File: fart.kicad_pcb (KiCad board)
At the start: 2 copper layers, 68.6 x 66 mm, 2 parts, among them U1 F3853, X1 CartConn

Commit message: PCB update
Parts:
- added REF**: MountingHole_5.3mm_M5, Mounting_Holes:MountingHole_5.3mm_M5, F.Cu at (118.1, 176.5)
- added REF**: MountingHole_5.3mm_M5, Mounting_Holes:MountingHole_5.3mm_M5, F.Cu at (184.2, 176.5)
- added REF**: MountingHole_5.3mm_M5, Mounting_Holes:MountingHole_5.3mm_M5, F.Cu at (184.2, 99.1)
- added REF**: MountingHole_5.3mm_M5, Mounting_Holes:MountingHole_5.3mm_M5, F.Cu at (118.1, 99.1)
- U1: moved to F.Cu
- moved X1 232.7 mm to (177.8, 67.9)
- moved U1 231.4 mm to (176.5, 95.2), turned to 270 degrees
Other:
- outline, holes or cut-outs redrawn

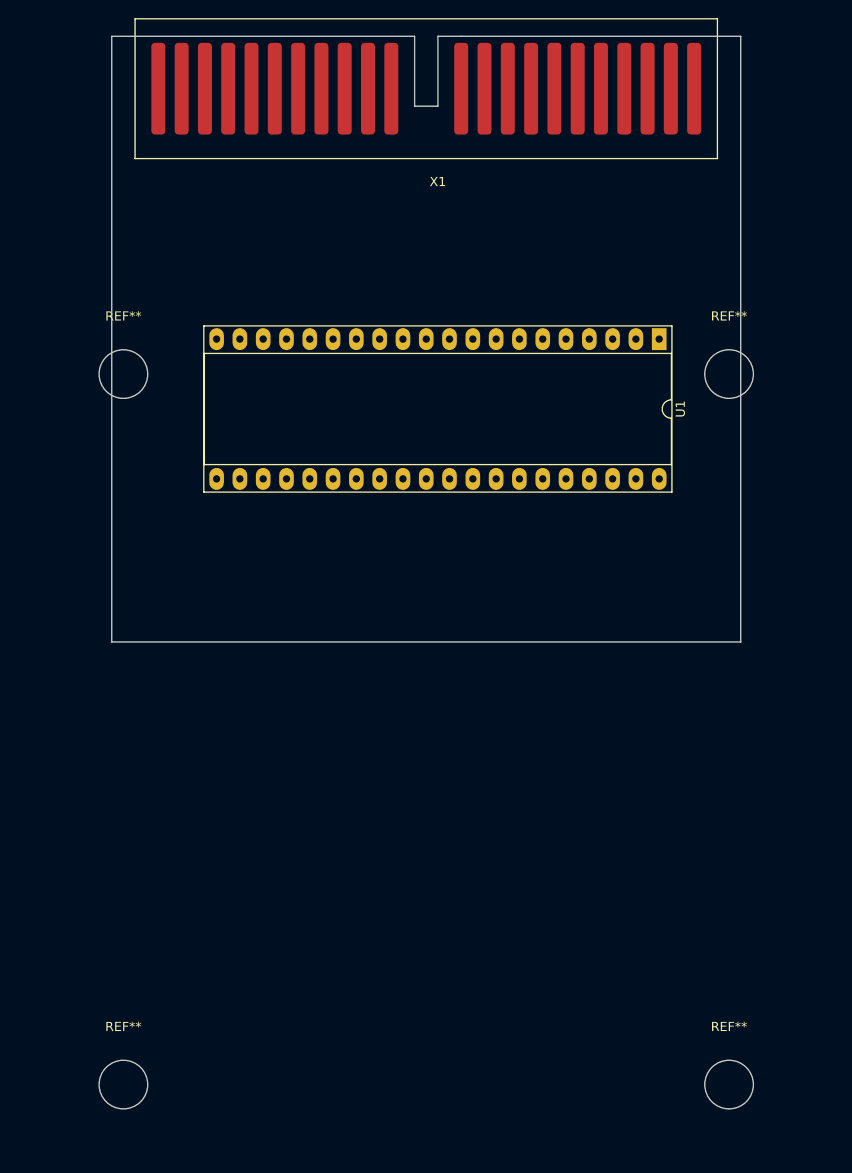
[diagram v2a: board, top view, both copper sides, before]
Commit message: Update PCB and socket 3d model
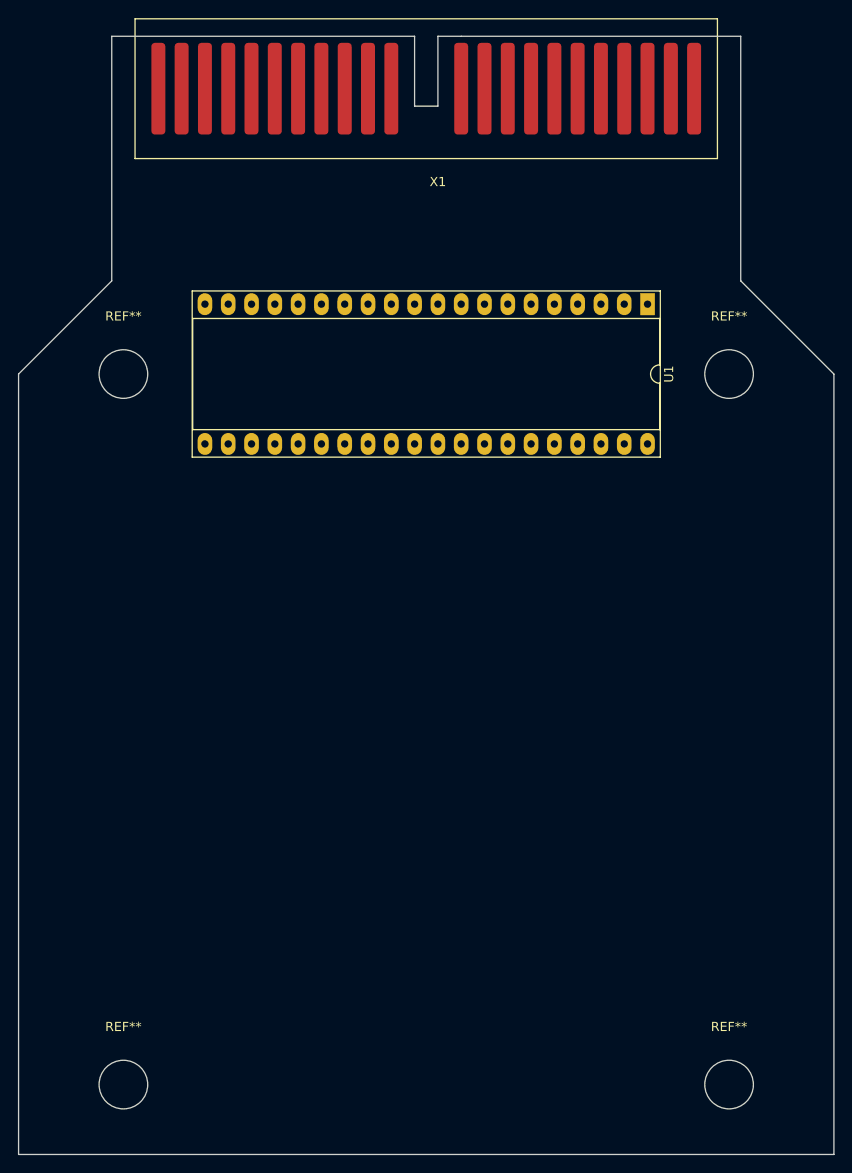
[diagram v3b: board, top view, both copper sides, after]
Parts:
- moved U1 4.02 mm to (175.3, 91.4)
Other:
- board size 68.6 x 66 mm -> 88.9 x 121.9 mm
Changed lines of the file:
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@@
-(kicad_pcb (version 20171130) (host pcbnew 5.1.2-f72e74a~84~ubuntu18.04.1)
+(kicad_pcb (version 20171130) (host pcbnew "(5.1.0)-1")
   (general
     (thickness 1.6)
-    (drawings 9)
+    (drawings 13)
     (tracks 0)
     (zones 0)
@@
   )
   (module Housings_DIP:DIP-40_W15.24mm_Socket_LongPads (layer F.Cu)
-    (at 176.53 95.25 270)
+    (at 175.26 91.44 270)
     (descr "40-lead though-hole mounted DIP package, row spacing 15.24 mm (600 mils), Socket, LongPads")
     (tags "THT DIP DIL PDIP 2.54mm 15.24mm 600mil Socket LongPads")
@@
       (rotate (xyz 0 0 0))
     )
+    (model ${KISYS3DMOD}/Package_DIP.3dshapes/DIP-40_W15.24mm_Socket.step
+      (at (xyz 0 0 0))
+      (scale (xyz 1 1 1))
+      (rotate (xyz 0 0 0))
+    )
   )
   (module fart:Cart_Conn (layer F.Cu)
@@
       (net 4 /ROMC3))
   )
+  (gr_line (start 106.68 99.06) (end 116.84 88.9) (layer Edge.Cuts) (width 0.05))
+  (gr_line (start 106.68 184.15) (end 106.68 99.06) (layer Edge.Cuts) (width 0.05))
+  (gr_line (start 195.58 184.15) (end 106.68 184.15) (layer Edge.Cuts) (width 0.05))
+  (gr_line (start 195.58 99.06) (end 195.58 184.15) (layer Edge.Cuts) (width 0.05))
+  (gr_line (start 185.42 88.9) (end 195.58 99.06) (layer Edge.Cuts) (width 0.05))
   (gr_line (start 152.4 62.23) (end 154.94 62.23) (layer Edge.Cuts) (width 0.05))
   (gr_line (start 152.4 69.85) (end 152.4 62.23) (layer Edge.Cuts) (width 0.05))
@@
   (gr_line (start 154.94 62.23) (end 185.42 62.23) (layer Edge.Cuts) (width 0.05))
   (gr_line (start 149.86 62.23) (end 149.86 69.85) (layer Edge.Cuts) (width 0.05))
-  (gr_line (start 116.84 128.27) (end 116.84 62.23) (layer Edge.Cuts) (width 0.05))
-  (gr_line (start 185.42 128.27) (end 116.84 128.27) (layer Edge.Cuts) (width 0.05))
-  (gr_line (start 185.42 62.23) (end 185.42 128.27) (layer Edge.Cuts) (width 0.05))
+  (gr_line (start 116.84 88.9) (end 116.84 62.23) (layer Edge.Cuts) (width 0.05))
+  (gr_line (start 185.42 62.23) (end 185.42 88.9) (layer Edge.Cuts) (width 0.05))
   (gr_line (start 116.84 62.23) (end 149.86 62.23) (layer Edge.Cuts) (width 0.05))
 )

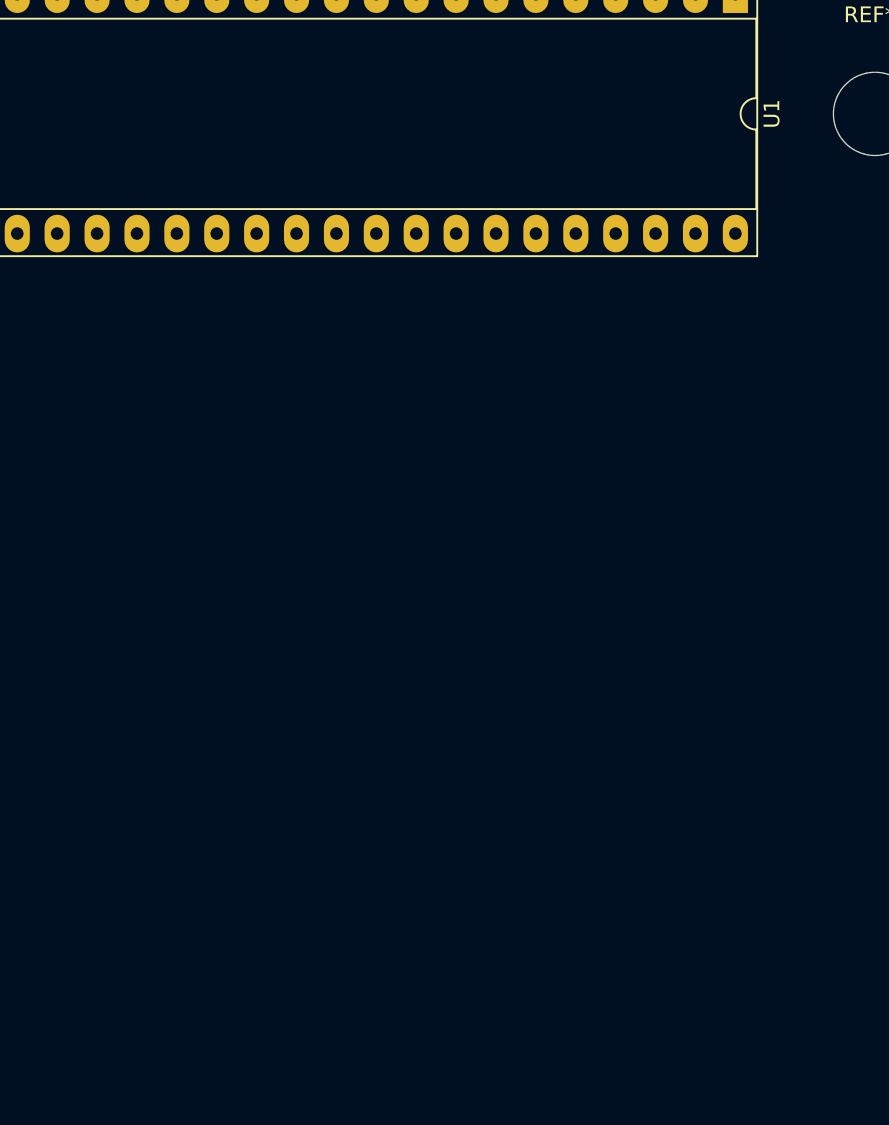
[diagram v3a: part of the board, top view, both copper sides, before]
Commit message: Add EEPROM and address decoder
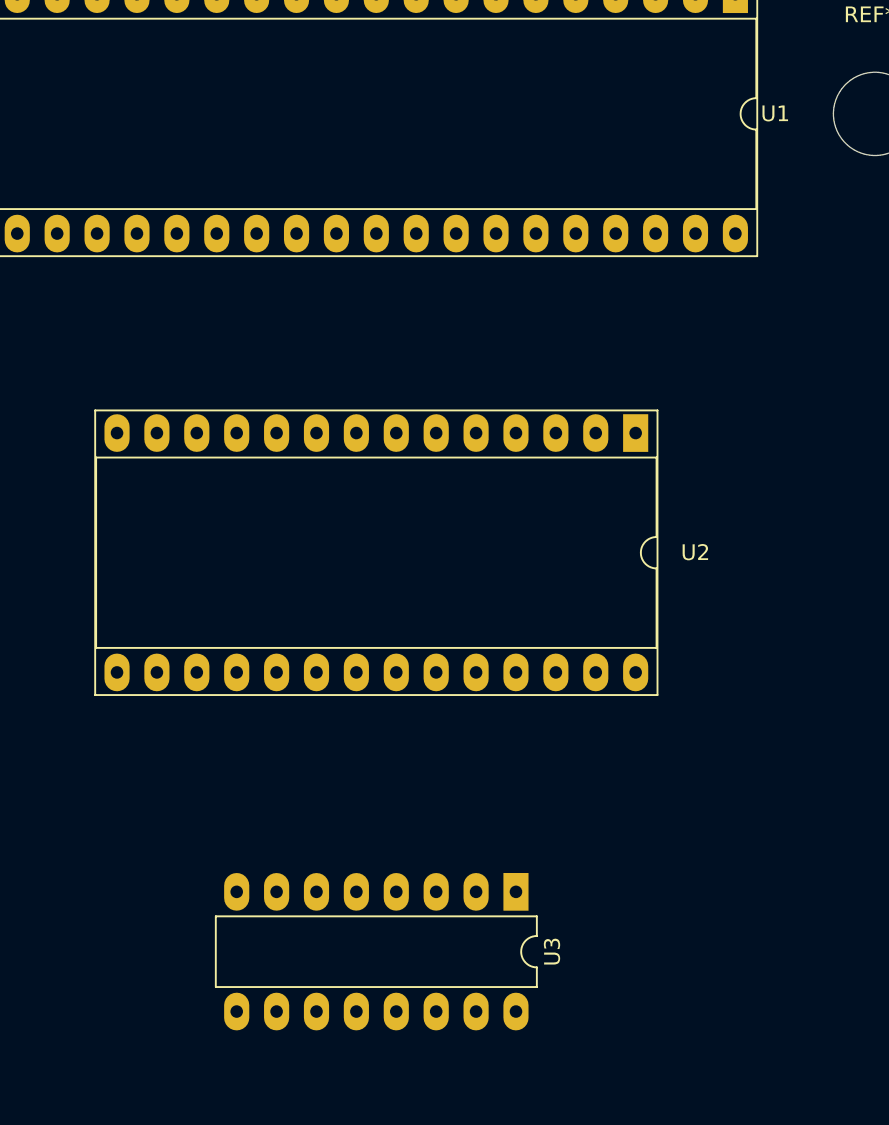
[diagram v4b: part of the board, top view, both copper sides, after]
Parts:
- added U2: AT28C64, Housings_DIP:DIP-28_W15.24mm_Socket_LongPads, F.Cu at (168.9, 119.4)
- added U3: 74156, Housings_DIP:DIP-16_W7.62mm_LongPads, F.Cu at (161.3, 148.6)

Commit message: Massive update
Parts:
- removed U2: AT28C64, Housings_DIP:DIP-28_W15.24mm_Socket_LongPads
- added U4: 74LS00, Housings_DIP:DIP-14_W7.62mm_Socket_LongPads, F.Cu at (121.9, 141.0)
- added U5: AT28C16, Housings_DIP:DIP-24_W15.24mm_Socket_LongPads, F.Cu at (144.8, 134.6)
- X1: moved to B.Cu
- moved U1 51.4 mm to (127.0, 109.2), turned to 90 degrees
- moved U3 47.1 mm to (119.4, 127.0), turned to 90 degrees
- moved X1 1.27 mm to (177.8, 69.2)
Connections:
- U1 pad 10: (no net) -> /A5
- U1 pad 11: (no net) -> /A4
- U1 pad 12: (no net) -> /A3
- U1 pad 13: (no net) -> /A2
- U1 pad 14: (no net) -> /A1
- U1 pad 15: (no net) -> /A0
- U1 pad 25: (no net) -> /A8
- U1 pad 26: (no net) -> /A9
- U1 pad 27: (no net) -> /A10
- U1 pad 28: (no net) -> /A11
- U1 pad 29: (no net) -> /A12
- U1 pad 30: (no net) -> /A13
- U1 pad 31: (no net) -> /A14
- U1 pad 32: (no net) -> /A15
- U1 pad 33: (no net) -> /REGDR
- U1 pad 34: (no net) -> /CPU_READ
- U1 pad 5: (no net) -> /~PRI_IN
- U1 pad 6: (no net) -> /~RAM_WRITE
- U1 pad 7: (no net) -> /~EXT_INT
- U1 pad 8: (no net) -> /A7
- U1 pad 9: (no net) -> /A6
- U3 pad 1: (no net) -> /A13
- U3 pad 10: (no net) -> /28xx
- U3 pad 11: (no net) -> /30xx
- U3 pad 12: (no net) -> /38xx
- U3 pad 13: (no net) -> /A11
- U3 pad 14: (no net) -> GND
- U3 pad 15: (no net) -> /A13
- U3 pad 2: (no net) -> GND
- U3 pad 3: (no net) -> /A12
- U3 pad 4: (no net) -> /18xx
- U3 pad 5: (no net) -> /10xx
- U3 pad 6: (no net) -> /08xx
- U3 pad 7: (no net) -> /00xx
- U3 pad 9: (no net) -> /20xx
- X1 pad 21: (no net) -> Net-(X1-Pad21)
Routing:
- net /WRITE: track 0.00 -> 59.5 mm, vias 0 -> 1
- net /D7: track 0.00 -> 56.0 mm, vias 0 -> 1
- net /D6: track 0.00 -> 55.6 mm, vias 0 -> 1
- net /D5: track 0.00 -> 55.3 mm, vias 0 -> 1
- net /D4: track 0.00 -> 52.4 mm, vias 0 -> 1
- net /PHI: track 0.00 -> 50.9 mm, vias 0 -> 1
- net /ROMC2: track 0.00 -> 48.8 mm, vias 0 -> 1
- net /ROMC3: track 0.00 -> 45.9 mm, vias 0 -> 1
- net /ROMC4: track 0.00 -> 35.3 mm, vias 0 -> 1
- net /D3: track 0.00 -> 33.0 mm, vias 0 -> 1
- net /~INTREQ: track 0.00 -> 6.35 mm, vias 0 -> 1
- net /ROMC1: track 0.00 -> 6.35 mm, vias 0 -> 1
- net /ROMC0: track 0.00 -> 6.35 mm, vias 0 -> 1
- net /D2: track 0.00 -> 6.35 mm, vias 0 -> 1
- net /D1: track 0.00 -> 6.35 mm, vias 0 -> 1
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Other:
- board size 88.9 x 121.9 mm -> 88.9 x 119.4 mm

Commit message: Rough routing done
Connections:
- U4 pad 1: /CPU_READ -> Net-(U4-Pad1)
- U4 pad 11: Net-(U4-Pad11) -> /~CPU_READ
- U4 pad 12: Net-(U4-Pad12) -> /CPU_READ
- U4 pad 13: Net-(U4-Pad13) -> /CPU_READ
- U4 pad 14: +5V -> (no net)
- U4 pad 2: /CPU_READ -> Net-(U4-Pad2)
- U4 pad 3: /~CPU_READ -> Net-(U4-Pad3)
- U4 pad 7: GND -> (no net)
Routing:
- net GND: track 0.00 -> 170.8 mm
- net +5V: track 0.00 -> 132.5 mm
- net /D2: track 6.35 -> 78.1 mm, vias 1 -> 2
- net /D0: track 6.35 -> 72.7 mm, vias 1 -> 2
- net /D1: track 6.35 -> 69.1 mm
- net /CPU_READ: track 0.00 -> 59.3 mm
- net /~INTREQ: track 6.35 -> 65.3 mm
- net /A13: track 0.00 -> 56.7 mm
- net /A12: track 0.00 -> 55.3 mm
- net /A11: track 0.00 -> 47.9 mm
- net +12V: track 0.00 -> 44.9 mm, vias 0 -> 2
- net /A8: track 0.00 -> 43.7 mm
- net /ROMC1: track 6.35 -> 46.9 mm
- net /ROMC0: track 6.35 -> 46.9 mm
- net /A9: track 0.00 -> 37.2 mm
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
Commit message: Update
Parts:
- added C1: 47uF 16V, Capacitors_THT:CP_Radial_D5.0mm_P2.50mm, F.Cu at (116.2, 135.9)
- added C5: 100nF, Capacitors_THT:C_Disc_D5.0mm_W2.5mm_P5.00mm, F.Cu at (141.0, 121.3)
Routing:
- net GND: track 170.8 -> 206.8 mm
- net +5V: track 132.5 -> 140.4 mm

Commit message: Add credentials
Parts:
- added REF**: SolderWirePad_single_0-8mmDrill, Wire_Pads:SolderWirePad_single_0-8mmDrill, F.Cu at (188.0, 109.2)
- added REF**: SolderWirePad_single_0-8mmDrill, Wire_Pads:SolderWirePad_single_0-8mmDrill, F.Cu at (182.9, 124.5)
- added REF**: SolderWirePad_single_0-8mmDrill, Wire_Pads:SolderWirePad_single_0-8mmDrill, F.Cu at (162.6, 170.2)
- added REF**: SolderWirePad_single_0-8mmDrill, Wire_Pads:SolderWirePad_single_0-8mmDrill, F.Cu at (165.1, 170.2)
- added REF**: SolderWirePad_single_0-8mmDrill, Wire_Pads:SolderWirePad_single_0-8mmDrill, F.Cu at (172.7, 170.2)
- added REF**: SolderWirePad_single_0-8mmDrill, Wire_Pads:SolderWirePad_single_0-8mmDrill, F.Cu at (160.0, 170.2)
- added REF**: SolderWirePad_single_0-8mmDrill, Wire_Pads:SolderWirePad_single_0-8mmDrill, F.Cu at (170.2, 170.2)
- added REF**: SolderWirePad_single_0-8mmDrill, Wire_Pads:SolderWirePad_single_0-8mmDrill, F.Cu at (129.5, 170.2)
- added REF**: SolderWirePad_single_0-8mmDrill, Wire_Pads:SolderWirePad_single_0-8mmDrill, F.Cu at (149.9, 170.2)
- added REF**: SolderWirePad_single_0-8mmDrill, Wire_Pads:SolderWirePad_single_0-8mmDrill, F.Cu at (132.1, 170.2)
- added REF**: SolderWirePad_single_0-8mmDrill, Wire_Pads:SolderWirePad_single_0-8mmDrill, F.Cu at (121.9, 170.2)
- added REF**: SolderWirePad_single_0-8mmDrill, Wire_Pads:SolderWirePad_single_0-8mmDrill, F.Cu at (134.6, 170.2)
- added REF**: SolderWirePad_single_0-8mmDrill, Wire_Pads:SolderWirePad_single_0-8mmDrill, F.Cu at (182.9, 116.8)
- added REF**: SolderWirePad_single_0-8mmDrill, Wire_Pads:SolderWirePad_single_0-8mmDrill, F.Cu at (154.9, 170.2)
- added REF**: SolderWirePad_single_0-8mmDrill, Wire_Pads:SolderWirePad_single_0-8mmDrill, F.Cu at (137.2, 170.2)
- added REF**: SolderWirePad_single_0-8mmDrill, Wire_Pads:SolderWirePad_single_0-8mmDrill, F.Cu at (144.8, 170.2)
- added REF**: SolderWirePad_single_0-8mmDrill, Wire_Pads:SolderWirePad_single_0-8mmDrill, F.Cu at (182.9, 137.2)
- added REF**: SolderWirePad_single_0-8mmDrill, Wire_Pads:SolderWirePad_single_0-8mmDrill, F.Cu at (190.5, 137.2)
- added REF**: SolderWirePad_single_0-8mmDrill, Wire_Pads:SolderWirePad_single_0-8mmDrill, F.Cu at (185.4, 137.2)
- added REF**: SolderWirePad_single_0-8mmDrill, Wire_Pads:SolderWirePad_single_0-8mmDrill, F.Cu at (188.0, 137.2)
- added REF**: SolderWirePad_single_0-8mmDrill, Wire_Pads:SolderWirePad_single_0-8mmDrill, F.Cu at (180.3, 137.2)
- added REF**: SolderWirePad_single_0-8mmDrill, Wire_Pads:SolderWirePad_single_0-8mmDrill, F.Cu at (185.4, 139.7)
- added REF**: SolderWirePad_single_0-8mmDrill, Wire_Pads:SolderWirePad_single_0-8mmDrill, F.Cu at (188.0, 139.7)
- added REF**: SolderWirePad_single_0-8mmDrill, Wire_Pads:SolderWirePad_single_0-8mmDrill, F.Cu at (185.4, 119.4)
- added REF**: SolderWirePad_single_0-8mmDrill, Wire_Pads:SolderWirePad_single_0-8mmDrill, F.Cu at (180.3, 139.7)
- added REF**: SolderWirePad_single_0-8mmDrill, Wire_Pads:SolderWirePad_single_0-8mmDrill, F.Cu at (190.5, 139.7)
- added REF**: SolderWirePad_single_0-8mmDrill, Wire_Pads:SolderWirePad_single_0-8mmDrill, F.Cu at (182.9, 139.7)
- added REF**: SolderWirePad_single_0-8mmDrill, Wire_Pads:SolderWirePad_single_0-8mmDrill, F.Cu at (180.3, 142.2)
- added REF**: SolderWirePad_single_0-8mmDrill, Wire_Pads:SolderWirePad_single_0-8mmDrill, F.Cu at (185.4, 142.2)
- added REF**: SolderWirePad_single_0-8mmDrill, Wire_Pads:SolderWirePad_single_0-8mmDrill, F.Cu at (182.9, 142.2)
- added REF**: SolderWirePad_single_0-8mmDrill, Wire_Pads:SolderWirePad_single_0-8mmDrill, F.Cu at (190.5, 142.2)
- added REF**: SolderWirePad_single_0-8mmDrill, Wire_Pads:SolderWirePad_single_0-8mmDrill, F.Cu at (188.0, 142.2)
- added REF**: SolderWirePad_single_0-8mmDrill, Wire_Pads:SolderWirePad_single_0-8mmDrill, F.Cu at (160.0, 144.8)
- added REF**: SolderWirePad_single_0-8mmDrill, Wire_Pads:SolderWirePad_single_0-8mmDrill, F.Cu at (182.9, 144.8)
- added REF**: SolderWirePad_single_0-8mmDrill, Wire_Pads:SolderWirePad_single_0-8mmDrill, F.Cu at (182.9, 114.3)
- added REF**: SolderWirePad_single_0-8mmDrill, Wire_Pads:SolderWirePad_single_0-8mmDrill, F.Cu at (167.6, 144.8)
- added REF**: SolderWirePad_single_0-8mmDrill, Wire_Pads:SolderWirePad_single_0-8mmDrill, F.Cu at (162.6, 144.8)
- added REF**: SolderWirePad_single_0-8mmDrill, Wire_Pads:SolderWirePad_single_0-8mmDrill, F.Cu at (177.8, 144.8)
- added REF**: SolderWirePad_single_0-8mmDrill, Wire_Pads:SolderWirePad_single_0-8mmDrill, F.Cu at (190.5, 144.8)
- added REF**: SolderWirePad_single_0-8mmDrill, Wire_Pads:SolderWirePad_single_0-8mmDrill, F.Cu at (152.4, 144.8)
- added REF**: SolderWirePad_single_0-8mmDrill, Wire_Pads:SolderWirePad_single_0-8mmDrill, F.Cu at (149.9, 144.8)
- added REF**: SolderWirePad_single_0-8mmDrill, Wire_Pads:SolderWirePad_single_0-8mmDrill, F.Cu at (157.5, 144.8)
- added REF**: SolderWirePad_single_0-8mmDrill, Wire_Pads:SolderWirePad_single_0-8mmDrill, F.Cu at (185.4, 144.8)
- added REF**: SolderWirePad_single_0-8mmDrill, Wire_Pads:SolderWirePad_single_0-8mmDrill, F.Cu at (154.9, 144.8)
- added REF**: SolderWirePad_single_0-8mmDrill, Wire_Pads:SolderWirePad_single_0-8mmDrill, F.Cu at (170.2, 144.8)
- added REF**: SolderWirePad_single_0-8mmDrill, Wire_Pads:SolderWirePad_single_0-8mmDrill, F.Cu at (188.0, 119.4)
- added REF**: SolderWirePad_single_0-8mmDrill, Wire_Pads:SolderWirePad_single_0-8mmDrill, F.Cu at (144.8, 144.8)
- added REF**: SolderWirePad_single_0-8mmDrill, Wire_Pads:SolderWirePad_single_0-8mmDrill, F.Cu at (165.1, 144.8)
- added REF**: SolderWirePad_single_0-8mmDrill, Wire_Pads:SolderWirePad_single_0-8mmDrill, F.Cu at (180.3, 144.8)
- added REF**: SolderWirePad_single_0-8mmDrill, Wire_Pads:SolderWirePad_single_0-8mmDrill, F.Cu at (147.3, 144.8)
- added REF**: SolderWirePad_single_0-8mmDrill, Wire_Pads:SolderWirePad_single_0-8mmDrill, F.Cu at (188.0, 144.8)
- added REF**: SolderWirePad_single_0-8mmDrill, Wire_Pads:SolderWirePad_single_0-8mmDrill, F.Cu at (172.7, 144.8)
- added REF**: SolderWirePad_single_0-8mmDrill, Wire_Pads:SolderWirePad_single_0-8mmDrill, F.Cu at (175.3, 144.8)
- added REF**: SolderWirePad_single_0-8mmDrill, Wire_Pads:SolderWirePad_single_0-8mmDrill, F.Cu at (175.3, 147.3)
- added REF**: SolderWirePad_single_0-8mmDrill, Wire_Pads:SolderWirePad_single_0-8mmDrill, F.Cu at (149.9, 147.3)
- added REF**: SolderWirePad_single_0-8mmDrill, Wire_Pads:SolderWirePad_single_0-8mmDrill, F.Cu at (144.8, 147.3)
- added REF**: SolderWirePad_single_0-8mmDrill, Wire_Pads:SolderWirePad_single_0-8mmDrill, F.Cu at (188.0, 114.3)
- added REF**: SolderWirePad_single_0-8mmDrill, Wire_Pads:SolderWirePad_single_0-8mmDrill, F.Cu at (167.6, 147.3)
- added REF**: SolderWirePad_single_0-8mmDrill, Wire_Pads:SolderWirePad_single_0-8mmDrill, F.Cu at (190.5, 147.3)
- added REF**: SolderWirePad_single_0-8mmDrill, Wire_Pads:SolderWirePad_single_0-8mmDrill, F.Cu at (154.9, 147.3)
- added REF**: SolderWirePad_single_0-8mmDrill, Wire_Pads:SolderWirePad_single_0-8mmDrill, F.Cu at (185.4, 147.3)
- added REF**: SolderWirePad_single_0-8mmDrill, Wire_Pads:SolderWirePad_single_0-8mmDrill, F.Cu at (172.7, 147.3)
- added REF**: SolderWirePad_single_0-8mmDrill, Wire_Pads:SolderWirePad_single_0-8mmDrill, F.Cu at (157.5, 147.3)
- added REF**: SolderWirePad_single_0-8mmDrill, Wire_Pads:SolderWirePad_single_0-8mmDrill, F.Cu at (177.8, 147.3)
- added REF**: SolderWirePad_single_0-8mmDrill, Wire_Pads:SolderWirePad_single_0-8mmDrill, F.Cu at (152.4, 147.3)
- added REF**: SolderWirePad_single_0-8mmDrill, Wire_Pads:SolderWirePad_single_0-8mmDrill, F.Cu at (162.6, 147.3)
- added REF**: SolderWirePad_single_0-8mmDrill, Wire_Pads:SolderWirePad_single_0-8mmDrill, F.Cu at (165.1, 147.3)
- added REF**: SolderWirePad_single_0-8mmDrill, Wire_Pads:SolderWirePad_single_0-8mmDrill, F.Cu at (190.5, 127.0)
- added REF**: SolderWirePad_single_0-8mmDrill, Wire_Pads:SolderWirePad_single_0-8mmDrill, F.Cu at (170.2, 147.3)
- added REF**: SolderWirePad_single_0-8mmDrill, Wire_Pads:SolderWirePad_single_0-8mmDrill, F.Cu at (160.0, 147.3)
- added REF**: SolderWirePad_single_0-8mmDrill, Wire_Pads:SolderWirePad_single_0-8mmDrill, F.Cu at (182.9, 147.3)
- added REF**: SolderWirePad_single_0-8mmDrill, Wire_Pads:SolderWirePad_single_0-8mmDrill, F.Cu at (147.3, 147.3)
- added REF**: SolderWirePad_single_0-8mmDrill, Wire_Pads:SolderWirePad_single_0-8mmDrill, F.Cu at (180.3, 147.3)
- added REF**: SolderWirePad_single_0-8mmDrill, Wire_Pads:SolderWirePad_single_0-8mmDrill, F.Cu at (188.0, 147.3)
- added REF**: SolderWirePad_single_0-8mmDrill, Wire_Pads:SolderWirePad_single_0-8mmDrill, F.Cu at (167.6, 152.4)
- added REF**: SolderWirePad_single_0-8mmDrill, Wire_Pads:SolderWirePad_single_0-8mmDrill, F.Cu at (177.8, 157.5)
- added REF**: SolderWirePad_single_0-8mmDrill, Wire_Pads:SolderWirePad_single_0-8mmDrill, F.Cu at (180.3, 167.6)
- added REF**: SolderWirePad_single_0-8mmDrill, Wire_Pads:SolderWirePad_single_0-8mmDrill, F.Cu at (162.6, 160.0)
- added REF**: SolderWirePad_single_0-8mmDrill, Wire_Pads:SolderWirePad_single_0-8mmDrill, F.Cu at (190.5, 116.8)
- added REF**: SolderWirePad_single_0-8mmDrill, Wire_Pads:SolderWirePad_single_0-8mmDrill, F.Cu at (177.8, 160.0)
- added REF**: SolderWirePad_single_0-8mmDrill, Wire_Pads:SolderWirePad_single_0-8mmDrill, F.Cu at (165.1, 154.9)
- added REF**: SolderWirePad_single_0-8mmDrill, Wire_Pads:SolderWirePad_single_0-8mmDrill, F.Cu at (188.0, 154.9)
- added REF**: SolderWirePad_single_0-8mmDrill, Wire_Pads:SolderWirePad_single_0-8mmDrill, F.Cu at (182.9, 157.5)
- added REF**: SolderWirePad_single_0-8mmDrill, Wire_Pads:SolderWirePad_single_0-8mmDrill, F.Cu at (185.4, 160.0)
- added REF**: SolderWirePad_single_0-8mmDrill, Wire_Pads:SolderWirePad_single_0-8mmDrill, F.Cu at (167.6, 160.0)
- added REF**: SolderWirePad_single_0-8mmDrill, Wire_Pads:SolderWirePad_single_0-8mmDrill, F.Cu at (154.9, 157.5)
- added REF**: SolderWirePad_single_0-8mmDrill, Wire_Pads:SolderWirePad_single_0-8mmDrill, F.Cu at (165.1, 167.6)
- added REF**: SolderWirePad_single_0-8mmDrill, Wire_Pads:SolderWirePad_single_0-8mmDrill, F.Cu at (157.5, 154.9)
- added REF**: SolderWirePad_single_0-8mmDrill, Wire_Pads:SolderWirePad_single_0-8mmDrill, F.Cu at (177.8, 162.6)
- added REF**: SolderWirePad_single_0-8mmDrill, Wire_Pads:SolderWirePad_single_0-8mmDrill, F.Cu at (185.4, 127.0)
- added REF**: SolderWirePad_single_0-8mmDrill, Wire_Pads:SolderWirePad_single_0-8mmDrill, F.Cu at (190.5, 160.0)
- added REF**: SolderWirePad_single_0-8mmDrill, Wire_Pads:SolderWirePad_single_0-8mmDrill, F.Cu at (165.1, 157.5)
- added REF**: SolderWirePad_single_0-8mmDrill, Wire_Pads:SolderWirePad_single_0-8mmDrill, F.Cu at (177.8, 154.9)
- added REF**: SolderWirePad_single_0-8mmDrill, Wire_Pads:SolderWirePad_single_0-8mmDrill, F.Cu at (190.5, 162.6)
- added REF**: SolderWirePad_single_0-8mmDrill, Wire_Pads:SolderWirePad_single_0-8mmDrill, F.Cu at (182.9, 167.6)
- added REF**: SolderWirePad_single_0-8mmDrill, Wire_Pads:SolderWirePad_single_0-8mmDrill, F.Cu at (157.5, 149.9)
- added REF**: SolderWirePad_single_0-8mmDrill, Wire_Pads:SolderWirePad_single_0-8mmDrill, F.Cu at (162.6, 157.5)
- added REF**: SolderWirePad_single_0-8mmDrill, Wire_Pads:SolderWirePad_single_0-8mmDrill, F.Cu at (160.0, 162.6)
- added REF**: SolderWirePad_single_0-8mmDrill, Wire_Pads:SolderWirePad_single_0-8mmDrill, F.Cu at (154.9, 154.9)
- added REF**: SolderWirePad_single_0-8mmDrill, Wire_Pads:SolderWirePad_single_0-8mmDrill, F.Cu at (152.4, 162.6)
- added REF**: SolderWirePad_single_0-8mmDrill, Wire_Pads:SolderWirePad_single_0-8mmDrill, F.Cu at (190.5, 129.5)
- added REF**: SolderWirePad_single_0-8mmDrill, Wire_Pads:SolderWirePad_single_0-8mmDrill, F.Cu at (154.9, 160.0)
- added REF**: SolderWirePad_single_0-8mmDrill, Wire_Pads:SolderWirePad_single_0-8mmDrill, F.Cu at (152.4, 160.0)
- added REF**: SolderWirePad_single_0-8mmDrill, Wire_Pads:SolderWirePad_single_0-8mmDrill, F.Cu at (177.8, 149.9)
- added REF**: SolderWirePad_single_0-8mmDrill, Wire_Pads:SolderWirePad_single_0-8mmDrill, F.Cu at (188.0, 167.6)
- added REF**: SolderWirePad_single_0-8mmDrill, Wire_Pads:SolderWirePad_single_0-8mmDrill, F.Cu at (157.5, 152.4)
- added REF**: SolderWirePad_single_0-8mmDrill, Wire_Pads:SolderWirePad_single_0-8mmDrill, F.Cu at (177.8, 152.4)
- added REF**: SolderWirePad_single_0-8mmDrill, Wire_Pads:SolderWirePad_single_0-8mmDrill, F.Cu at (165.1, 162.6)
- added REF**: SolderWirePad_single_0-8mmDrill, Wire_Pads:SolderWirePad_single_0-8mmDrill, F.Cu at (154.9, 165.1)
- added REF**: SolderWirePad_single_0-8mmDrill, Wire_Pads:SolderWirePad_single_0-8mmDrill, F.Cu at (160.0, 165.1)
- added REF**: SolderWirePad_single_0-8mmDrill, Wire_Pads:SolderWirePad_single_0-8mmDrill, F.Cu at (175.3, 152.4)
- added REF**: SolderWirePad_single_0-8mmDrill, Wire_Pads:SolderWirePad_single_0-8mmDrill, F.Cu at (190.5, 111.8)
- added REF**: SolderWirePad_single_0-8mmDrill, Wire_Pads:SolderWirePad_single_0-8mmDrill, F.Cu at (182.9, 134.6)
- added REF**: SolderWirePad_single_0-8mmDrill, Wire_Pads:SolderWirePad_single_0-8mmDrill, F.Cu at (160.0, 154.9)
- added REF**: SolderWirePad_single_0-8mmDrill, Wire_Pads:SolderWirePad_single_0-8mmDrill, F.Cu at (172.7, 154.9)
- added REF**: SolderWirePad_single_0-8mmDrill, Wire_Pads:SolderWirePad_single_0-8mmDrill, F.Cu at (188.0, 152.4)
- added REF**: SolderWirePad_single_0-8mmDrill, Wire_Pads:SolderWirePad_single_0-8mmDrill, F.Cu at (190.5, 154.9)
- added REF**: SolderWirePad_single_0-8mmDrill, Wire_Pads:SolderWirePad_single_0-8mmDrill, F.Cu at (175.3, 149.9)
- added REF**: SolderWirePad_single_0-8mmDrill, Wire_Pads:SolderWirePad_single_0-8mmDrill, F.Cu at (190.5, 149.9)
- added REF**: SolderWirePad_single_0-8mmDrill, Wire_Pads:SolderWirePad_single_0-8mmDrill, F.Cu at (157.5, 167.6)
- added REF**: SolderWirePad_single_0-8mmDrill, Wire_Pads:SolderWirePad_single_0-8mmDrill, F.Cu at (162.6, 152.4)
- added REF**: SolderWirePad_single_0-8mmDrill, Wire_Pads:SolderWirePad_single_0-8mmDrill, F.Cu at (172.7, 149.9)
- added REF**: SolderWirePad_single_0-8mmDrill, Wire_Pads:SolderWirePad_single_0-8mmDrill, F.Cu at (162.6, 165.1)
- added REF**: SolderWirePad_single_0-8mmDrill, Wire_Pads:SolderWirePad_single_0-8mmDrill, F.Cu at (185.4, 129.5)
- added REF**: SolderWirePad_single_0-8mmDrill, Wire_Pads:SolderWirePad_single_0-8mmDrill, F.Cu at (170.2, 162.6)
- added REF**: SolderWirePad_single_0-8mmDrill, Wire_Pads:SolderWirePad_single_0-8mmDrill, F.Cu at (172.7, 152.4)
- added REF**: SolderWirePad_single_0-8mmDrill, Wire_Pads:SolderWirePad_single_0-8mmDrill, F.Cu at (185.4, 152.4)
- added REF**: SolderWirePad_single_0-8mmDrill, Wire_Pads:SolderWirePad_single_0-8mmDrill, F.Cu at (154.9, 149.9)
- added REF**: SolderWirePad_single_0-8mmDrill, Wire_Pads:SolderWirePad_single_0-8mmDrill, F.Cu at (160.0, 149.9)
- added REF**: SolderWirePad_single_0-8mmDrill, Wire_Pads:SolderWirePad_single_0-8mmDrill, F.Cu at (167.6, 165.1)
- added REF**: SolderWirePad_single_0-8mmDrill, Wire_Pads:SolderWirePad_single_0-8mmDrill, F.Cu at (185.4, 157.5)
- added REF**: SolderWirePad_single_0-8mmDrill, Wire_Pads:SolderWirePad_single_0-8mmDrill, F.Cu at (167.6, 154.9)
- added REF**: SolderWirePad_single_0-8mmDrill, Wire_Pads:SolderWirePad_single_0-8mmDrill, F.Cu at (172.7, 160.0)
- added REF**: SolderWirePad_single_0-8mmDrill, Wire_Pads:SolderWirePad_single_0-8mmDrill, F.Cu at (152.4, 154.9)
- added REF**: SolderWirePad_single_0-8mmDrill, Wire_Pads:SolderWirePad_single_0-8mmDrill, F.Cu at (182.9, 129.5)
- added REF**: SolderWirePad_single_0-8mmDrill, Wire_Pads:SolderWirePad_single_0-8mmDrill, F.Cu at (167.6, 157.5)
- added REF**: SolderWirePad_single_0-8mmDrill, Wire_Pads:SolderWirePad_single_0-8mmDrill, F.Cu at (185.4, 149.9)
- added REF**: SolderWirePad_single_0-8mmDrill, Wire_Pads:SolderWirePad_single_0-8mmDrill, F.Cu at (188.0, 165.1)
- added REF**: SolderWirePad_single_0-8mmDrill, Wire_Pads:SolderWirePad_single_0-8mmDrill, F.Cu at (177.8, 165.1)
- added REF**: SolderWirePad_single_0-8mmDrill, Wire_Pads:SolderWirePad_single_0-8mmDrill, F.Cu at (172.7, 162.6)
- added REF**: SolderWirePad_single_0-8mmDrill, Wire_Pads:SolderWirePad_single_0-8mmDrill, F.Cu at (170.2, 165.1)
- added REF**: SolderWirePad_single_0-8mmDrill, Wire_Pads:SolderWirePad_single_0-8mmDrill, F.Cu at (167.6, 167.6)
- added REF**: SolderWirePad_single_0-8mmDrill, Wire_Pads:SolderWirePad_single_0-8mmDrill, F.Cu at (170.2, 157.5)
- added REF**: SolderWirePad_single_0-8mmDrill, Wire_Pads:SolderWirePad_single_0-8mmDrill, F.Cu at (152.4, 167.6)
- added REF**: SolderWirePad_single_0-8mmDrill, Wire_Pads:SolderWirePad_single_0-8mmDrill, F.Cu at (175.3, 165.1)
- added REF**: SolderWirePad_single_0-8mmDrill, Wire_Pads:SolderWirePad_single_0-8mmDrill, F.Cu at (190.5, 124.5)
- added REF**: SolderWirePad_single_0-8mmDrill, Wire_Pads:SolderWirePad_single_0-8mmDrill, F.Cu at (182.9, 162.6)
- added REF**: SolderWirePad_single_0-8mmDrill, Wire_Pads:SolderWirePad_single_0-8mmDrill, F.Cu at (152.4, 157.5)
- added REF**: SolderWirePad_single_0-8mmDrill, Wire_Pads:SolderWirePad_single_0-8mmDrill, F.Cu at (154.9, 167.6)
- added REF**: SolderWirePad_single_0-8mmDrill, Wire_Pads:SolderWirePad_single_0-8mmDrill, F.Cu at (175.3, 162.6)
- added REF**: SolderWirePad_single_0-8mmDrill, Wire_Pads:SolderWirePad_single_0-8mmDrill, F.Cu at (152.4, 165.1)
- added REF**: SolderWirePad_single_0-8mmDrill, Wire_Pads:SolderWirePad_single_0-8mmDrill, F.Cu at (154.9, 162.6)
- added REF**: SolderWirePad_single_0-8mmDrill, Wire_Pads:SolderWirePad_single_0-8mmDrill, F.Cu at (190.5, 165.1)
- added REF**: SolderWirePad_single_0-8mmDrill, Wire_Pads:SolderWirePad_single_0-8mmDrill, F.Cu at (152.4, 149.9)
- added REF**: SolderWirePad_single_0-8mmDrill, Wire_Pads:SolderWirePad_single_0-8mmDrill, F.Cu at (170.2, 167.6)
- added REF**: SolderWirePad_single_0-8mmDrill, Wire_Pads:SolderWirePad_single_0-8mmDrill, F.Cu at (182.9, 160.0)
- added REF**: SolderWirePad_single_0-8mmDrill, Wire_Pads:SolderWirePad_single_0-8mmDrill, F.Cu at (185.4, 132.1)
- added REF**: SolderWirePad_single_0-8mmDrill, Wire_Pads:SolderWirePad_single_0-8mmDrill, F.Cu at (190.5, 167.6)
- added REF**: SolderWirePad_single_0-8mmDrill, Wire_Pads:SolderWirePad_single_0-8mmDrill, F.Cu at (160.0, 157.5)
- added REF**: SolderWirePad_single_0-8mmDrill, Wire_Pads:SolderWirePad_single_0-8mmDrill, F.Cu at (175.3, 154.9)
- added REF**: SolderWirePad_single_0-8mmDrill, Wire_Pads:SolderWirePad_single_0-8mmDrill, F.Cu at (180.3, 160.0)
- added REF**: SolderWirePad_single_0-8mmDrill, Wire_Pads:SolderWirePad_single_0-8mmDrill, F.Cu at (165.1, 165.1)
- added REF**: SolderWirePad_single_0-8mmDrill, Wire_Pads:SolderWirePad_single_0-8mmDrill, F.Cu at (185.4, 154.9)
- added REF**: SolderWirePad_single_0-8mmDrill, Wire_Pads:SolderWirePad_single_0-8mmDrill, F.Cu at (188.0, 162.6)
- added REF**: SolderWirePad_single_0-8mmDrill, Wire_Pads:SolderWirePad_single_0-8mmDrill, F.Cu at (180.3, 165.1)
- added REF**: SolderWirePad_single_0-8mmDrill, Wire_Pads:SolderWirePad_single_0-8mmDrill, F.Cu at (180.3, 152.4)
- added REF**: SolderWirePad_single_0-8mmDrill, Wire_Pads:SolderWirePad_single_0-8mmDrill, F.Cu at (172.7, 167.6)
- added REF**: SolderWirePad_single_0-8mmDrill, Wire_Pads:SolderWirePad_single_0-8mmDrill, F.Cu at (188.0, 129.5)
- added REF**: SolderWirePad_single_0-8mmDrill, Wire_Pads:SolderWirePad_single_0-8mmDrill, F.Cu at (180.3, 157.5)
- added REF**: SolderWirePad_single_0-8mmDrill, Wire_Pads:SolderWirePad_single_0-8mmDrill, F.Cu at (170.2, 149.9)
- added REF**: SolderWirePad_single_0-8mmDrill, Wire_Pads:SolderWirePad_single_0-8mmDrill, F.Cu at (172.7, 157.5)
- added REF**: SolderWirePad_single_0-8mmDrill, Wire_Pads:SolderWirePad_single_0-8mmDrill, F.Cu at (162.6, 167.6)
- added REF**: SolderWirePad_single_0-8mmDrill, Wire_Pads:SolderWirePad_single_0-8mmDrill, F.Cu at (182.9, 154.9)
- added REF**: SolderWirePad_single_0-8mmDrill, Wire_Pads:SolderWirePad_single_0-8mmDrill, F.Cu at (182.9, 149.9)
- added REF**: SolderWirePad_single_0-8mmDrill, Wire_Pads:SolderWirePad_single_0-8mmDrill, F.Cu at (190.5, 152.4)
- added REF**: SolderWirePad_single_0-8mmDrill, Wire_Pads:SolderWirePad_single_0-8mmDrill, F.Cu at (175.3, 167.6)
- added REF**: SolderWirePad_single_0-8mmDrill, Wire_Pads:SolderWirePad_single_0-8mmDrill, F.Cu at (180.3, 162.6)
- added REF**: SolderWirePad_single_0-8mmDrill, Wire_Pads:SolderWirePad_single_0-8mmDrill, F.Cu at (160.0, 167.6)
- added REF**: SolderWirePad_single_0-8mmDrill, Wire_Pads:SolderWirePad_single_0-8mmDrill, F.Cu at (185.4, 116.8)
- added REF**: SolderWirePad_single_0-8mmDrill, Wire_Pads:SolderWirePad_single_0-8mmDrill, F.Cu at (188.0, 149.9)
- added REF**: SolderWirePad_single_0-8mmDrill, Wire_Pads:SolderWirePad_single_0-8mmDrill, F.Cu at (157.5, 160.0)
- added REF**: SolderWirePad_single_0-8mmDrill, Wire_Pads:SolderWirePad_single_0-8mmDrill, F.Cu at (175.3, 157.5)
- added REF**: SolderWirePad_single_0-8mmDrill, Wire_Pads:SolderWirePad_single_0-8mmDrill, F.Cu at (182.9, 152.4)
- added REF**: SolderWirePad_single_0-8mmDrill, Wire_Pads:SolderWirePad_single_0-8mmDrill, F.Cu at (188.0, 160.0)
- added REF**: SolderWirePad_single_0-8mmDrill, Wire_Pads:SolderWirePad_single_0-8mmDrill, F.Cu at (170.2, 160.0)
- added REF**: SolderWirePad_single_0-8mmDrill, Wire_Pads:SolderWirePad_single_0-8mmDrill, F.Cu at (165.1, 149.9)
- added REF**: SolderWirePad_single_0-8mmDrill, Wire_Pads:SolderWirePad_single_0-8mmDrill, F.Cu at (167.6, 162.6)
- added REF**: SolderWirePad_single_0-8mmDrill, Wire_Pads:SolderWirePad_single_0-8mmDrill, F.Cu at (162.6, 149.9)
- added REF**: SolderWirePad_single_0-8mmDrill, Wire_Pads:SolderWirePad_single_0-8mmDrill, F.Cu at (154.9, 152.4)
- added REF**: SolderWirePad_single_0-8mmDrill, Wire_Pads:SolderWirePad_single_0-8mmDrill, F.Cu at (182.9, 132.1)
- added REF**: SolderWirePad_single_0-8mmDrill, Wire_Pads:SolderWirePad_single_0-8mmDrill, F.Cu at (160.0, 152.4)
- added REF**: SolderWirePad_single_0-8mmDrill, Wire_Pads:SolderWirePad_single_0-8mmDrill, F.Cu at (152.4, 152.4)
- added REF**: SolderWirePad_single_0-8mmDrill, Wire_Pads:SolderWirePad_single_0-8mmDrill, F.Cu at (170.2, 152.4)
- added REF**: SolderWirePad_single_0-8mmDrill, Wire_Pads:SolderWirePad_single_0-8mmDrill, F.Cu at (165.1, 152.4)
- added REF**: SolderWirePad_single_0-8mmDrill, Wire_Pads:SolderWirePad_single_0-8mmDrill, F.Cu at (157.5, 162.6)
- added REF**: SolderWirePad_single_0-8mmDrill, Wire_Pads:SolderWirePad_single_0-8mmDrill, F.Cu at (165.1, 160.0)
- added REF**: SolderWirePad_single_0-8mmDrill, Wire_Pads:SolderWirePad_single_0-8mmDrill, F.Cu at (162.6, 154.9)
- added REF**: SolderWirePad_single_0-8mmDrill, Wire_Pads:SolderWirePad_single_0-8mmDrill, F.Cu at (177.8, 167.6)
- added REF**: SolderWirePad_single_0-8mmDrill, Wire_Pads:SolderWirePad_single_0-8mmDrill, F.Cu at (157.5, 157.5)
- added REF**: SolderWirePad_single_0-8mmDrill, Wire_Pads:SolderWirePad_single_0-8mmDrill, F.Cu at (170.2, 154.9)
- added REF**: SolderWirePad_single_0-8mmDrill, Wire_Pads:SolderWirePad_single_0-8mmDrill, F.Cu at (185.4, 114.3)
- added REF**: SolderWirePad_single_0-8mmDrill, Wire_Pads:SolderWirePad_single_0-8mmDrill, F.Cu at (182.9, 165.1)
- added REF**: SolderWirePad_single_0-8mmDrill, Wire_Pads:SolderWirePad_single_0-8mmDrill, F.Cu at (180.3, 149.9)
- added REF**: SolderWirePad_single_0-8mmDrill, Wire_Pads:SolderWirePad_single_0-8mmDrill, F.Cu at (190.5, 157.5)
- added REF**: SolderWirePad_single_0-8mmDrill, Wire_Pads:SolderWirePad_single_0-8mmDrill, F.Cu at (188.0, 157.5)
- added REF**: SolderWirePad_single_0-8mmDrill, Wire_Pads:SolderWirePad_single_0-8mmDrill, F.Cu at (157.5, 165.1)
- added REF**: SolderWirePad_single_0-8mmDrill, Wire_Pads:SolderWirePad_single_0-8mmDrill, F.Cu at (185.4, 162.6)
- added REF**: SolderWirePad_single_0-8mmDrill, Wire_Pads:SolderWirePad_single_0-8mmDrill, F.Cu at (160.0, 160.0)
- added REF**: SolderWirePad_single_0-8mmDrill, Wire_Pads:SolderWirePad_single_0-8mmDrill, F.Cu at (185.4, 167.6)
- added REF**: SolderWirePad_single_0-8mmDrill, Wire_Pads:SolderWirePad_single_0-8mmDrill, F.Cu at (175.3, 160.0)
- added REF**: SolderWirePad_single_0-8mmDrill, Wire_Pads:SolderWirePad_single_0-8mmDrill, F.Cu at (172.7, 165.1)
- added REF**: SolderWirePad_single_0-8mmDrill, Wire_Pads:SolderWirePad_single_0-8mmDrill, F.Cu at (185.4, 121.9)
- added REF**: SolderWirePad_single_0-8mmDrill, Wire_Pads:SolderWirePad_single_0-8mmDrill, F.Cu at (167.6, 149.9)
- added REF**: SolderWirePad_single_0-8mmDrill, Wire_Pads:SolderWirePad_single_0-8mmDrill, F.Cu at (180.3, 154.9)
- added REF**: SolderWirePad_single_0-8mmDrill, Wire_Pads:SolderWirePad_single_0-8mmDrill, F.Cu at (162.6, 162.6)
- added REF**: SolderWirePad_single_0-8mmDrill, Wire_Pads:SolderWirePad_single_0-8mmDrill, F.Cu at (185.4, 165.1)
- added REF**: SolderWirePad_single_0-8mmDrill, Wire_Pads:SolderWirePad_single_0-8mmDrill, F.Cu at (147.3, 152.4)
- added REF**: SolderWirePad_single_0-8mmDrill, Wire_Pads:SolderWirePad_single_0-8mmDrill, F.Cu at (142.2, 160.0)
- added REF**: SolderWirePad_single_0-8mmDrill, Wire_Pads:SolderWirePad_single_0-8mmDrill, F.Cu at (144.8, 154.9)
- added REF**: SolderWirePad_single_0-8mmDrill, Wire_Pads:SolderWirePad_single_0-8mmDrill, F.Cu at (147.3, 160.0)
- added REF**: SolderWirePad_single_0-8mmDrill, Wire_Pads:SolderWirePad_single_0-8mmDrill, F.Cu at (134.6, 157.5)
- added REF**: SolderWirePad_single_0-8mmDrill, Wire_Pads:SolderWirePad_single_0-8mmDrill, F.Cu at (144.8, 167.6)
- added REF**: SolderWirePad_single_0-8mmDrill, Wire_Pads:SolderWirePad_single_0-8mmDrill, F.Cu at (185.4, 111.8)
- added REF**: SolderWirePad_single_0-8mmDrill, Wire_Pads:SolderWirePad_single_0-8mmDrill, F.Cu at (188.0, 116.8)
- added REF**: SolderWirePad_single_0-8mmDrill, Wire_Pads:SolderWirePad_single_0-8mmDrill, F.Cu at (137.2, 154.9)
- added REF**: SolderWirePad_single_0-8mmDrill, Wire_Pads:SolderWirePad_single_0-8mmDrill, F.Cu at (144.8, 157.5)
- added REF**: SolderWirePad_single_0-8mmDrill, Wire_Pads:SolderWirePad_single_0-8mmDrill, F.Cu at (137.2, 149.9)
- added REF**: SolderWirePad_single_0-8mmDrill, Wire_Pads:SolderWirePad_single_0-8mmDrill, F.Cu at (142.2, 157.5)
- added REF**: SolderWirePad_single_0-8mmDrill, Wire_Pads:SolderWirePad_single_0-8mmDrill, F.Cu at (139.7, 162.6)
- added REF**: SolderWirePad_single_0-8mmDrill, Wire_Pads:SolderWirePad_single_0-8mmDrill, F.Cu at (134.6, 154.9)
- added REF**: SolderWirePad_single_0-8mmDrill, Wire_Pads:SolderWirePad_single_0-8mmDrill, F.Cu at (132.1, 162.6)
- added REF**: SolderWirePad_single_0-8mmDrill, Wire_Pads:SolderWirePad_single_0-8mmDrill, F.Cu at (134.6, 160.0)
- added REF**: SolderWirePad_single_0-8mmDrill, Wire_Pads:SolderWirePad_single_0-8mmDrill, F.Cu at (132.1, 160.0)
- added REF**: SolderWirePad_single_0-8mmDrill, Wire_Pads:SolderWirePad_single_0-8mmDrill, F.Cu at (137.2, 152.4)
- added REF**: SolderWirePad_single_0-8mmDrill, Wire_Pads:SolderWirePad_single_0-8mmDrill, F.Cu at (185.4, 124.5)
- added REF**: SolderWirePad_single_0-8mmDrill, Wire_Pads:SolderWirePad_single_0-8mmDrill, F.Cu at (144.8, 162.6)
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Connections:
- U4 pad 14: (no net) -> +5V
- U4 pad 7: (no net) -> GND
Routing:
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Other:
- board text added: "2019 tnt23"
